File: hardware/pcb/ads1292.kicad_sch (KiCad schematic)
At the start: 14 parts, among them J5 ECG, U8 ADS1292RIPBSR

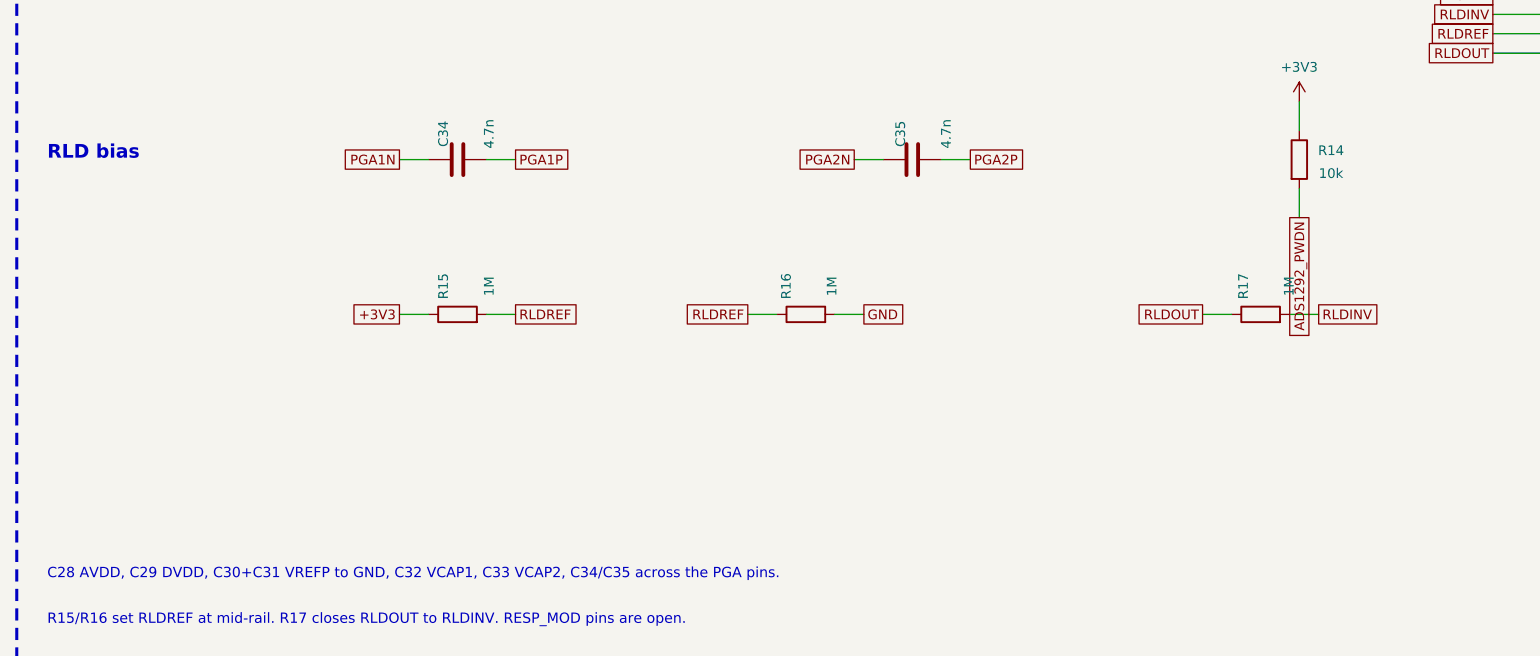
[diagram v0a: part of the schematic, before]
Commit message: Hide silk designators and separate colliding schematic labels.
Reference and value silk is hidden so 0402 designators no longer overlap pads. The AD5940, AFE4900, and ADS1292 sheets are spaced so net names clear the symbols above them. The part list is unchanged.

Co-authored-by: Riyu-D1 <Riyu-D1@users.noreply.github.com>
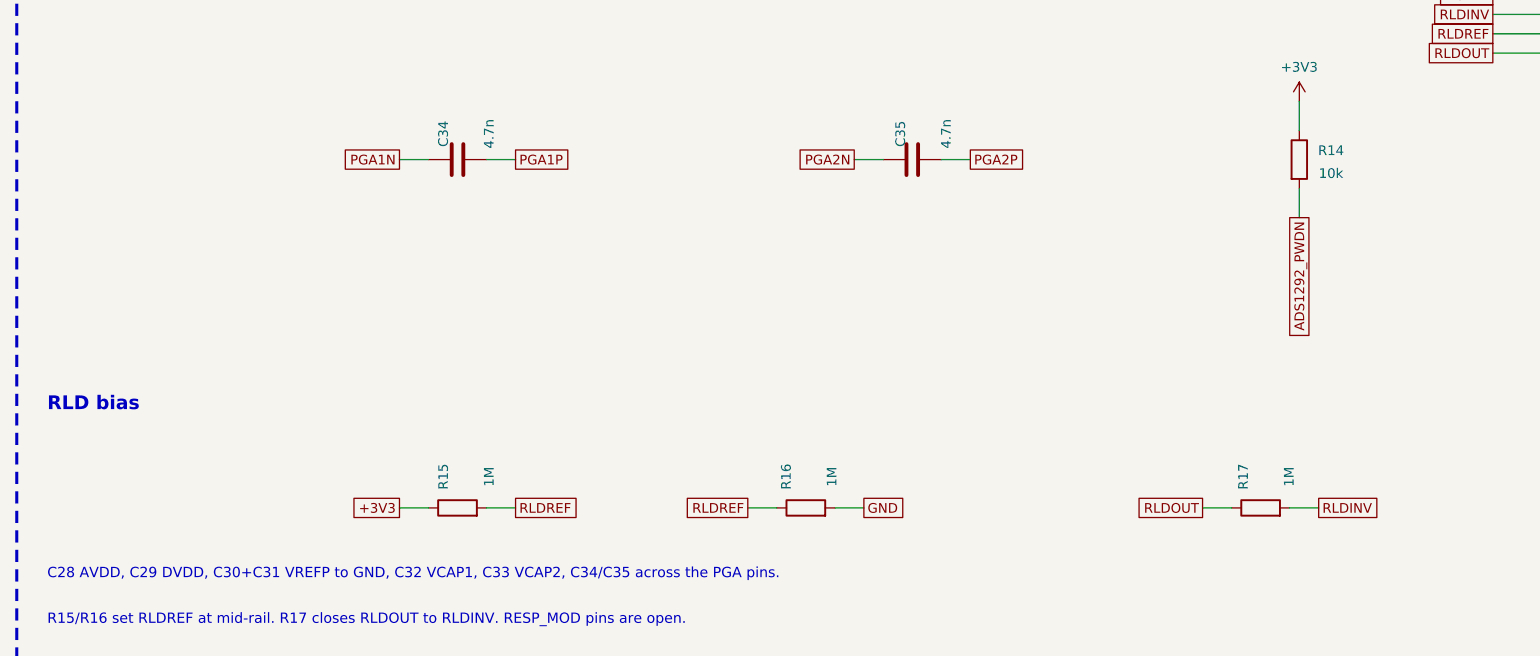
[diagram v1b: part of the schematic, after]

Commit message: Use official CAD and shrink the hw_v1 board to 37x30 mm.
Replace the hand-drawn AFE4900, AD5940, ADS1292R, AS7341, MLX90632,
TMP117, LSM6DSV80X, and MCP73831 symbols and footprints with the
SnapMagic and Ultra Librarian libraries. ADS1292R is now the QFN-32
ADS1292RIRSMT, and MLX90632SLD-DCB-100-SP moves SDA/SCL onto the
existing 1.8 V bus. Pin headers and mounting holes are flat solder
pads. The unrouted 4-layer placement keeps the antenna on the left
edge and the skin sensors together on the bottom.

Co-authored-by: Riyu-D1 <Riyu-D1@users.noreply.github.com>
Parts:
- removed U8: ADS1292RIPBSR, Package_QFP:TQFP-32_5x5mm_P0.5mm, symbol vitalq:ADS1292RIPBSR
- added U8: ADS1292RIRSMT, snap:QFN40P400X400X100-33N-D, symbol vitalq:ADS1292RIRSMT
- J5: value ECG -> ECG pads; footprint Connector_PinHeader_1.27mm:PinHeader_1x03_P1.27mm_Horizontal -> vitalq:Pads_ECG
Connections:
- net +3V3: now also U8.12 (AVDD), U8.14 (CLKSEL), U8.23 (DVDD)
- net ADS1292_DRDY: now also U8.22 (~{DRDY})
- net ADS1292_PWDN: now also U8.15 (~{PWDN}/~{RESET})
- net ADS1292_START: now also U8.16 (START)
- net CS_ADS1292: now also U8.18 (~{CS})
- net GND: now also U8.10 (VREFN), U8.13 (AVSS), U8.24 (DGND), U8.33 (EP)
- net IN1N: now also U8.3 (IN1N), U8.5 (IN2N)
- net IN1P: now also U8.4 (IN1P), U8.6 (IN2P)
- net PGA1N: now also U8.1 (PGA1N)
- net PGA1P: now also U8.2 (PGA1P)
- net PGA2N: now also U8.7 (PGA2N)
- net PGA2P: now also U8.8 (PGA2P)
- net RLDINV: now also U8.28 (RLDINV)
- net RLDOUT: now also U8.30 (RLDOUT)
- net RLDREF: now also U8.29 (RLDIN/RLDREF)
- net SPI_MISO: now also U8.21 (DOUT)
- net SPI_MOSI: now also U8.19 (DIN)
- net SPI_SCK: now also U8.20 (SCLK)
- net VCAP1: now also U8.11 (VCAP1)
- net VCAP2: now also U8.27 (VCAP2)
- net VREFP: now also U8.9 (VREFP)
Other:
- note added: "J5 solder pads: 1 IN1P 2 IN1N 3 RLDOUT. No header."
- note added: "QFN-32 RSM, not the TQFP. Exposed pad pin 33 is AVSS. C28 AVDD, C29 DVDD, C30+C31 VREFP, C32 VCAP1, C33 VCAP2."
- note removed: "C28 AVDD, C29 DVDD, C30+C31 VREFP to GND, C32 VCAP1, C33 VCAP2, C34/C35 across the PGA pins."
- note removed: "CLKSEL is tied to DVDD. The CLK pin is open. IN2P/IN2N share the IN1 nets so channel 2 is not floating."
- note removed: "J5 1 IN1P 2 IN1N 3 RLDOUT"
- note removed: "PWDN is pulled up. Hold digital inputs low until the supplies are up if the datasheet timing is required."

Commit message: Pack the hw_v1 board to 36.2 x 28 mm and correct the 3D models.
The LSM6 body is a 3.0 x 2.5 x 0.83 mm box in KiCad VRML units, and the other vendor models are rotated so they stand on their lands. Skin sensors sit in one bottom cluster with the electrode pads around them, bypass parts are packed next to their ICs outside the antenna keep-out, and the schematic frames clear the title block.

Co-authored-by: Riyu-D1 <Riyu-D1@users.noreply.github.com>
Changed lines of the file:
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@@
 		(instances
 			(project "vitalq_hw_v1"
-				(path "/3a03f3a2-f664-49ab-a6e3-0e34faafa582/22451261-5d59-4a22-addc-dfa41087bf08"
+				(path "/6fcf6b13-4a8e-4f25-a8b9-d34cb547168d/03fbae81-463f-4e06-8a23-1f0819a0bbcb"
 					(reference "U8")
 					(unit 1)
@@
 		(instances
 			(project "vitalq_hw_v1"
-				(path "/3a03f3a2-f664-49ab-a6e3-0e34faafa582/22451261-5d59-4a22-addc-dfa41087bf08"
+				(path "/6fcf6b13-4a8e-4f25-a8b9-d34cb547168d/03fbae81-463f-4e06-8a23-1f0819a0bbcb"
 					(reference "#PWR066")
 					(unit 1)
@@
 		(instances
 			(project "vitalq_hw_v1"
-				(path "/3a03f3a2-f664-49ab-a6e3-0e34faafa582/22451261-5d59-4a22-addc-dfa41087bf08"
+				(path "/6fcf6b13-4a8e-4f25-a8b9-d34cb547168d/03fbae81-463f-4e06-8a23-1f0819a0bbcb"
 					(reference "#PWR067")
 					(unit 1)
@@
 	(symbol
 		(lib_id "vitalq:Conn_01x03_Pin")
-		(at 48.26 39.37 0)
+		(at 48.26 55.88 0)
 		(unit 1)
 		(exclude_from_sim no)
@@
 		(dnp no)
 		(property "Reference" "J5"
-			(at 53.34 28.83 0)
+			(at 53.34 45.34 0)
 			(effects (font (size 1.27 1.27)))
 		)
 		(property "Value" "ECG pads"
-			(at 53.34 47.91 0)
+			(at 53.34 64.42 0)
 			(effects (font (size 1.27 1.27)))
 		)
 		(property "Footprint" "vitalq:Pads_ECG"
-			(at 48.26 39.37 0)
-			(effects (font (size 1.27 1.27)) (hide yes))
-		)
-		(property "Datasheet" ""
-			(at 48.26 39.37 0)
+			(at 48.26 55.88 0)
+			(effects (font (size 1.27 1.27)) (hide yes))
+		)
+		(property "Datasheet" ""
+			(at 48.26 55.88 0)
 			(effects (font (size 1.27 1.27)) (hide yes))
 		)
@@
 		(instances
 			(project "vitalq_hw_v1"
-				(path "/3a03f3a2-f664-49ab-a6e3-0e34faafa582/22451261-5d59-4a22-addc-dfa41087bf08"
+				(path "/6fcf6b13-4a8e-4f25-a8b9-d34cb547168d/03fbae81-463f-4e06-8a23-1f0819a0bbcb"
 					(reference "J5")
 					(unit 1)
@@
 		(instances
 			(project "vitalq_hw_v1"
-				(path "/3a03f3a2-f664-49ab-a6e3-0e34faafa582/22451261-5d59-4a22-addc-dfa41087bf08"
+				(path "/6fcf6b13-4a8e-4f25-a8b9-d34cb547168d/03fbae81-463f-4e06-8a23-1f0819a0bbcb"
 					(reference "C28")
 					(unit 1)
@@
 		(instances
 			(project "vitalq_hw_v1"
-				(path "/3a03f3a2-f664-49ab-a6e3-0e34faafa582/22451261-5d59-4a22-addc-dfa41087bf08"
+				(path "/6fcf6b13-4a8e-4f25-a8b9-d34cb547168d/03fbae81-463f-4e06-8a23-1f0819a0bbcb"
 					(reference "#PWR068")
 					(unit 1)
@@
 		(instances
 			(project "vitalq_hw_v1"
-				(path "/3a03f3a2-f664-49ab-a6e3-0e34faafa582/22451261-5d59-4a22-addc-dfa41087bf08"
+				(path "/6fcf6b13-4a8e-4f25-a8b9-d34cb547168d/03fbae81-463f-4e06-8a23-1f0819a0bbcb"
 					(reference "#PWR069")
 					(unit 1)
@@
 		(instances
 			(project "vitalq_hw_v1"
-				(path "/3a03f3a2-f664-49ab-a6e3-0e34faafa582/22451261-5d59-4a22-addc-dfa41087bf08"
+				(path "/6fcf6b13-4a8e-4f25-a8b9-d34cb547168d/03fbae81-463f-4e06-8a23-1f0819a0bbcb"
 					(reference "C29")
 					(unit 1)
@@
 		(instances
 			(project "vitalq_hw_v1"
-				(path "/3a03f3a2-f664-49ab-a6e3-0e34faafa582/22451261-5d59-4a22-addc-dfa41087bf08"
+				(path "/6fcf6b13-4a8e-4f25-a8b9-d34cb547168d/03fbae81-463f-4e06-8a23-1f0819a0bbcb"
 					(reference "#PWR070")
 					(unit 1)
@@
 		(instances
 			(project "vitalq_hw_v1"
-				(path "/3a03f3a2-f664-49ab-a6e3-0e34faafa582/22451261-5d59-4a22-addc-dfa41087bf08"
+				(path "/6fcf6b13-4a8e-4f25-a8b9-d34cb547168d/03fbae81-463f-4e06-8a23-1f0819a0bbcb"
 					(reference "#PWR071")
 					(unit 1)
@@
 		(instances
 			(project "vitalq_hw_v1"
-				(path "/3a03f3a2-f664-49ab-a6e3-0e34faafa582/22451261-5d59-4a22-addc-dfa41087bf08"
+				(path "/6fcf6b13-4a8e-4f25-a8b9-d34cb547168d/03fbae81-463f-4e06-8a23-1f0819a0bbcb"
 					(reference "C30")
 					(unit 1)
@@
 		(instances
 			(project "vitalq_hw_v1"
-				(path "/3a03f3a2-f664-49ab-a6e3-0e34faafa582/22451261-5d59-4a22-addc-dfa41087bf08"
+				(path "/6fcf6b13-4a8e-4f25-a8b9-d34cb547168d/03fbae81-463f-4e06-8a23-1f0819a0bbcb"
 					(reference "#PWR072")
 					(unit 1)
@@
 		(instances
 			(project "vitalq_hw_v1"
-				(path "/3a03f3a2-f664-49ab-a6e3-0e34faafa582/22451261-5d59-4a22-addc-dfa41087bf08"
+				(path "/6fcf6b13-4a8e-4f25-a8b9-d34cb547168d/03fbae81-463f-4e06-8a23-1f0819a0bbcb"
 					(reference "C31")
 					(unit 1)
@@
 		(instances
 			(project "vitalq_hw_v1"
-				(path "/3a03f3a2-f664-49ab-a6e3-0e34faafa582/22451261-5d59-4a22-addc-dfa41087bf08"
+				(path "/6fcf6b13-4a8e-4f25-a8b9-d34cb547168d/03fbae81-463f-4e06-8a23-1f0819a0bbcb"
 					(reference "#PWR073")
 					(unit 1)
@@
 		(instances
 			(project "vitalq_hw_v1"
-				(path "/3a03f3a2-f664-49ab-a6e3-0e34faafa582/22451261-5d59-4a22-addc-dfa41087bf08"
+				(path "/6fcf6b13-4a8e-4f25-a8b9-d34cb547168d/03fbae81-463f-4e06-8a23-1f0819a0bbcb"
 					(reference "C32")
 					(unit 1)
@@
 		(instances
 			(project "vitalq_hw_v1"
-				(path "/3a03f3a2-f664-49ab-a6e3-0e34faafa582/22451261-5d59-4a22-addc-dfa41087bf08"
+				(path "/6fcf6b13-4a8e-4f25-a8b9-d34cb547168d/03fbae81-463f-4e06-8a23-1f0819a0bbcb"
 					(reference "#PWR074")
 					(unit 1)
@@
 		(instances
 			(project "vitalq_hw_v1"
-				(path "/3a03f3a2-f664-49ab-a6e3-0e34faafa582/22451261-5d59-4a22-addc-dfa41087bf08"
+				(path "/6fcf6b13-4a8e-4f25-a8b9-d34cb547168d/03fbae81-463f-4e06-8a23-1f0819a0bbcb"
 					(reference "C33")
 					(unit 1)
@@
 		(instances
 			(project "vitalq_hw_v1"
-				(path "/3a03f3a2-f664-49ab-a6e3-0e34faafa582/22451261-5d59-4a22-addc-dfa41087bf08"
+				(path "/6fcf6b13-4a8e-4f25-a8b9-d34cb547168d/03fbae81-463f-4e06-8a23-1f0819a0bbcb"
 					(reference "#PWR075")
 					(unit 1)
@@
 		(instances
 			(project "vitalq_hw_v1"
-				(path "/3a03f3a2-f664-49ab-a6e3-0e34faafa582/22451261-5d59-4a22-addc-dfa41087bf08"
+				(path "/6fcf6b13-4a8e-4f25-a8b9-d34cb547168d/03fbae81-463f-4e06-8a23-1f0819a0bbcb"
 					(reference "C34")
 					(unit 1)
@@
 		(instances
 			(project "vitalq_hw_v1"
-				(path "/3a03f3a2-f664-49ab-a6e3-0e34faafa582/22451261-5d59-4a22-addc-dfa41087bf08"
+				(path "/6fcf6b13-4a8e-4f25-a8b9-d34cb547168d/03fbae81-463f-4e06-8a23-1f0819a0bbcb"
 					(reference "C35")
 					(unit 1)
@@
 		(instances
 			(project "vitalq_hw_v1"
-				(path "/3a03f3a2-f664-49ab-a6e3-0e34faafa582/22451261-5d59-4a22-addc-dfa41087bf08"
+				(path "/6fcf6b13-4a8e-4f25-a8b9-d34cb547168d/03fbae81-463f-4e06-8a23-1f0819a0bbcb"
 					(reference "R14")
 					(unit 1)
@@
 		(instances
 			(project "vitalq_hw_v1"
-				(path "/3a03f3a2-f664-49ab-a6e3-0e34faafa582/22451261-5d59-4a22-addc-dfa41087bf08"
+				(path "/6fcf6b13-4a8e-4f25-a8b9-d34cb547168d/03fbae81-463f-4e06-8a23-1f0819a0bbcb"
 					(reference "#PWR076")
 					(unit 1)
@@
 		(instances
 			(project "vitalq_hw_v1"
-				(path "/3a03f3a2-f664-49ab-a6e3-0e34faafa582/22451261-5d59-4a22-addc-dfa41087bf08"
+				(path "/6fcf6b13-4a8e-4f25-a8b9-d34cb547168d/03fbae81-463f-4e06-8a23-1f0819a0bbcb"
 					(reference "R15")
 					(unit 1)
@@
 		(instances
 			(project "vitalq_hw_v1"
-				(path "/3a03f3a2-f664-49ab-a6e3-0e34faafa582/22451261-5d59-4a22-addc-dfa41087bf08"
+				(path "/6fcf6b13-4a8e-4f25-a8b9-d34cb547168d/03fbae81-463f-4e06-8a23-1f0819a0bbcb"
 					(reference "R16")
 					(unit 1)
@@
 		(instances
 			(project "vitalq_hw_v1"
-				(path "/3a03f3a2-f664-49ab-a6e3-0e34faafa582/22451261-5d59-4a22-addc-dfa41087bf08"
+				(path "/6fcf6b13-4a8e-4f25-a8b9-d34cb547168d/03fbae81-463f-4e06-8a23-1f0819a0bbcb"
 					(reference "R17")
 					(unit 1)
@@
 	)
 	(rectangle
-		(start 12.0 16.0)
-		(end 408.0 258.0)
+		(start 12.0 40.0)
+		(end 406.0 258.0)
 		(stroke (width 0.4) (type dash))
 		(fill (type none))
@@
 	(wire
 		(pts
-			(xy 53.34 36.83)
-			(xy 60.96 36.83)
+			(xy 53.34 53.34)
+			(xy 60.96 53.34)
 		)
 		(stroke (width 0) (type default))
@@
 	(global_label "IN1P"
 		(shape passive)
-		(at 60.96 36.83 0)
-		(effects (font (size 1.27 1.27)) (justify left))
-		(property "Intersheetrefs" "${INTERSHEET_REFS}"
-			(at 60.96 36.83 0)
-			(effects (font (size 1.27 1.27)) (hide yes))
-		)
-	)
-	(wire
-		(pts
-			(xy 53.34 39.37)
-			(xy 60.96 39.37)
+		(at 60.96 53.34 0)
+		(effects (font (size 1.27 1.27)) (justify left))
+		(property "Intersheetrefs" "${INTERSHEET_REFS}"
+			(at 60.96 53.34 0)
+			(effects (font (size 1.27 1.27)) (hide yes))
+		)
+	)
+	(wire
+		(pts
+			(xy 53.34 55.88)
+			(xy 60.96 55.88)
 		)
 		(stroke (width 0) (type default))
@@
 	(global_label "IN1N"
 		(shape passive)
-		(at 60.96 39.37 0)
-		(effects (font (size 1.27 1.27)) (justify left))
-		(property "Intersheetrefs" "${INTERSHEET_REFS}"
-			(at 60.96 39.37 0)
-			(effects (font (size 1.27 1.27)) (hide yes))
-		)
-	)
-	(wire
-		(pts
-			(xy 53.34 41.91)
-			(xy 60.96 41.91)
+		(at 60.96 55.88 0)
+		(effects (font (size 1.27 1.27)) (justify left))
+		(property "Intersheetrefs" "${INTERSHEET_REFS}"
+			(at 60.96 55.88 0)
+			(effects (font (size 1.27 1.27)) (hide yes))
+		)
+	)
+	(wire
+		(pts
+			(xy 53.34 58.42)
+			(xy 60.96 58.42)
 		)
 		(stroke (width 0) (type default))
@@
 	(global_label "RLDOUT"
 		(shape passive)
-		(at 60.96 41.91 0)
-		(effects (font (size 1.27 1.27)) (justify left))
-		(property "Intersheetrefs" "${INTERSHEET_REFS}"
-			(at 60.96 41.91 0)
+		(at 60.96 58.42 0)
+		(effects (font (size 1.27 1.27)) (justify left))
+		(property "Intersheetrefs" "${INTERSHEET_REFS}"
+			(at 60.96 58.42 0)
 			(effects (font (size 1.27 1.27)) (hide yes))
 		)
@@
 	(text "J5 solder pads: 1 IN1P  2 IN1N  3 RLDOUT. No header."
 		(exclude_from_sim no)
-		(at 16.0 28.0 0)
+		(at 16.0 44.0 0)
 		(effects (font (size 1.4 1.4)) (justify left bottom))
 	)

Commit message: Seat the QFN models and drop passives the datasheets do not require.
The ADS1292R STEP is already Z-up, so the extra X rotation stood the
4x4x1 mm body on edge. Remove TP1, TP2, C5, C12, C17, C31 and R4, add
the 1 uF AVDD bulk capacitor, and shorten the outline to 36.2 x 27.8 mm.

Co-authored-by: Riyu-D1 <Riyu-D1@users.noreply.github.com>
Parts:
- removed C31: 100n, Capacitor_SMD:C_0402_1005Metric, symbol vitalq:C
- added C43: 1u, Capacitor_SMD:C_0402_1005Metric, symbol vitalq:C
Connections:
- net +3V3: now also C43.1
- net GND: now also C43.2
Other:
- note added: "C29 is DVDD, C30 is VREFP, C32 is VCAP1, C33 is VCAP2. R15/R16 set RLDREF. R17 closes the RLD loop."
- note added: "QFN-32 RSM. Pad 33 is AVSS. C43 is the 1 uF AVDD bulk (SBAS502 11.1), C28 the 100 nF beside it."
- note removed: "QFN-32 RSM, not the TQFP. Exposed pad pin 33 is AVSS. C28 AVDD, C29 DVDD, C30+C31 VREFP, C32 VCAP1, C33 VCAP2."
- note removed: "R15/R16 set RLDREF at mid-rail. R17 closes RLDOUT to RLDINV. RESP_MOD pins are open."

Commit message: Add the chest-board sensors and replace the 3.3 V LDO with a TPS63802.
The unrouted 40 x 34 mm board keeps every previous part except the off-board PPG pads, which the SFH 7072 replaces. Respiration, a second ECG lead, electrode protection, EDA, fuel gauge, flash, and the I/O expander are in the schematic.

Co-authored-by: Riyu-D1 <Riyu-D1@users.noreply.github.com>
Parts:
- removed J5: ECG pads, vitalq:Pads_ECG, symbol vitalq:Conn_01x03_Pin
- added C48, C49, C52, C53: 2.2n, Capacitor_SMD:C_0402_1005Metric, symbol vitalq:C
- added C50, C51: 100n, Capacitor_SMD:C_0402_1005Metric, symbol vitalq:C
- added D1, D2, D3, D4, D5: TPD1E10B06, vitalq:TPD1E10B06_DPY, symbol vitalq:D_TVS_2
- added J5: ECG pads, vitalq:Pads_ECG, symbol vitalq:Conn_01x05_Pin
- added R26, R27, R28, R29: 10M, Resistor_SMD:R_0402_1005Metric, symbol vitalq:R
- added R30, R31: 40.2k, Resistor_SMD:R_0402_1005Metric, symbol vitalq:R
- added R32, R33, R34, R35, R36: 49.9k, Resistor_SMD:R_0402_1005Metric, symbol vitalq:R
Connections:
- net ADS1292_START is gone; now on net GND: U8.16 (START)
- net +3V3: now also R26.1, R28.1; no longer R14.1
- net ADS1292_PWDN: now also R14.1; no longer R14.2
- net GND: now also R14.2, C48.2, C49.2, C52.2, C53.2, D1.2, D2.2, D3.2, D4.2, D5.2, R27.2, R29.2
- net IN1N: now also C49.1, C51.2, R28.2, R29.1; no longer U8.5 (IN2N)
- net IN1P: now also C48.1, C50.2, R26.2, R27.1; no longer U8.6 (IN2P)
- net RLDOUT: now also R34.2
- net RESP_MODP: now reaches U8.31 (RESP_MODP/IN3P)
- net RESP_MODP: now also R30.1
- net RESP_MODN: now reaches U8.32 (RESP_MODN/IN3N)
- net RESP_MODN: now also R31.1
- new net AFE_N_AC: R36.2
- new net AFE_N_PAD: D5.1, J5.5 (Pin_5), R36.1
- new net AFE_P_AC: R35.2
- new net AFE_P_PAD: D4.1, J5.4 (Pin_4), R35.1
- new net ECG1_PAD: D1.1, J5.1 (Pin_1), R32.1
- new net ECG2_PAD: D2.1, J5.2 (Pin_2), R33.1
- new net ECG_N: C51.1, C53.1, R31.2, R33.2, U8.5 (IN2N)
- new net ECG_P: C50.1, C52.1, R30.2, R32.2, U8.6 (IN2P)
- new net RLD_PAD: D3.1, J5.3 (Pin_3), R34.1
- no-connect marks 5 -> 3
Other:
- note added: "ADS1292R ECG and respiration"
- note added: "Channel 1 is respiration (SBAS502C Fig 68). Channel 2 is the ECG lead. START is tied low."
- note added: "J5 flat pads: 1 ADS+ 2 ADS- 3 RLD 4 AFE+ 5 AFE-. No header."
- note removed: "ADS1292R ECG"
- note removed: "C29 is DVDD, C30 is VREFP, C32 is VCAP1, C33 is VCAP2. R15/R16 set RLDREF. R17 closes the RLD loop."
- note removed: "Channel 2 is tied to channel 1. Respiration components are not fitted."
- note removed: "J5 solder pads: 1 IN1P 2 IN1N 3 RLDOUT. No header."
- note removed: "QFN-32 RSM. Pad 33 is AVSS. C43 is the 1 uF AVDD bulk (SBAS502 11.1), C28 the 100 nF beside it."

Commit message: Cluster the skin sensors and set the respiration filter to 47 nF.
Stack U20 on top of U11, shrink the outline to 36.5 x 32 mm, and give the AFE4900 a generic WCSP body so it shows in the render.

Co-authored-by: Riyu-D1 <Riyu-D1@users.noreply.github.com>
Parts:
- C34: value 4.7n -> 47n
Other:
- note added: "C34 is 47 nF: Fig 73 note (1), required when channel 1 respiration is on."
